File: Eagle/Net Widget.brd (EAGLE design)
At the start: 76.2 x 45.7 mm, 19 parts, among them IC1 ATmega1284P

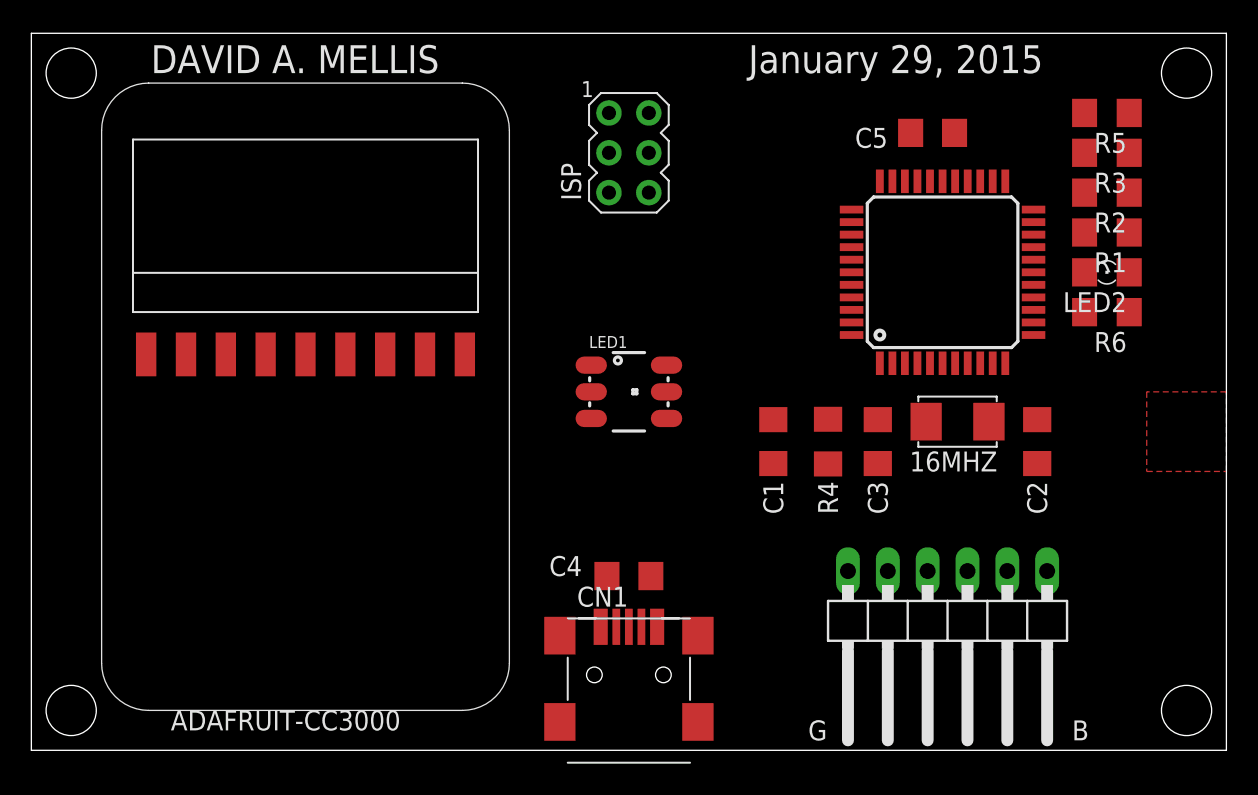
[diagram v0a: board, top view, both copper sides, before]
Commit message: Re-arrange LEDs and touch point.
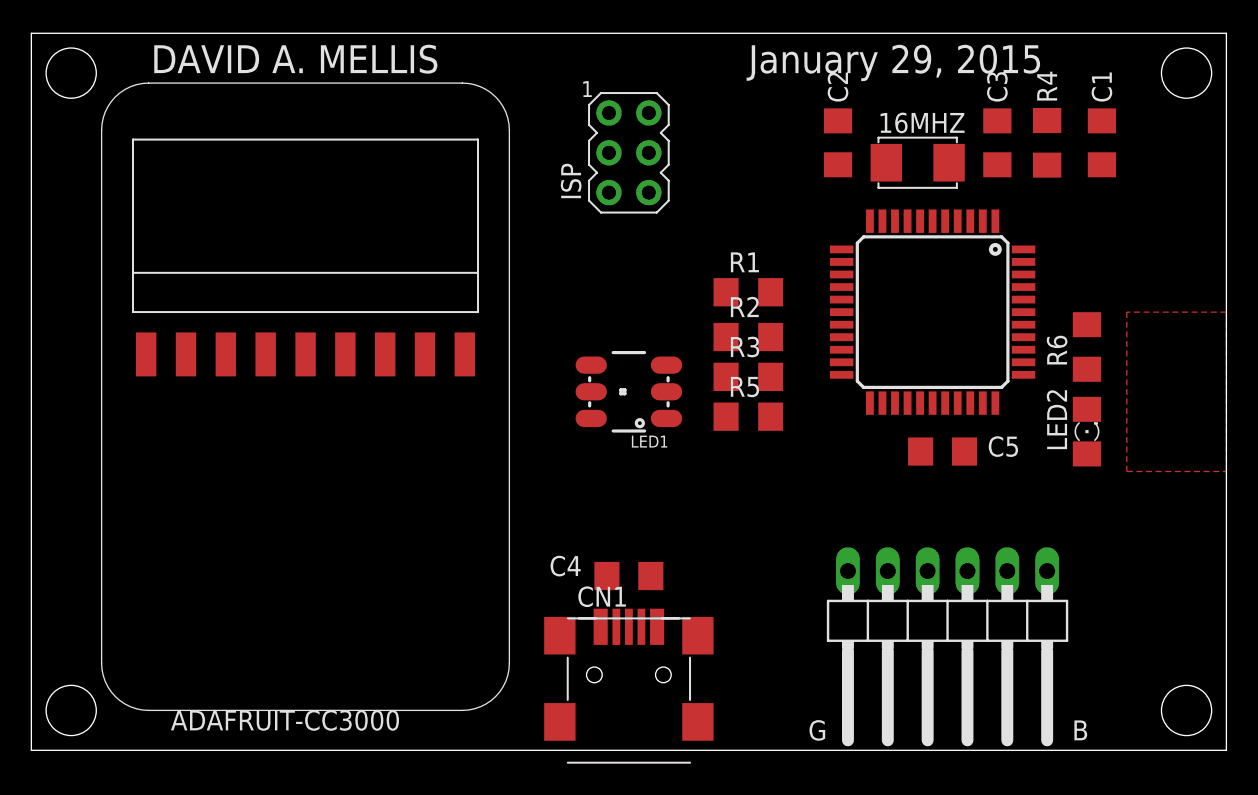
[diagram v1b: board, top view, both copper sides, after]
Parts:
- moved R5 30.0 mm to (45.7, 21.3), turned to 0 degrees
- moved C1 28.3 mm to (68.3, 38.7), turned to 90 degrees
- moved R3 27.0 mm to (45.7, 23.8), turned to 0 degrees
- moved R2 24.6 mm to (45.7, 26.4), turned to 0 degrees
- moved R4 23.6 mm to (64.8, 38.7), turned to 90 degrees
- moved R1 23.2 mm to (45.7, 29.2), turned to 0 degrees
- moved C2 22.9 mm to (51.4, 38.7), turned to 270 degrees
- moved C3 20.5 mm to (61.6, 38.7), turned to 270 degrees
- moved C5 20.3 mm to (58.1, 19.1), turned to 0 degrees
- moved 16MHZ 16.7 mm to (56.5, 37.5), turned to 0 degrees
- moved LED2 10.2 mm to (67.3, 20.3), turned to 90 degrees
- moved IC1 2.62 mm to (57.5, 27.9), turned to 270 degrees
- moved R6 2.56 mm to (67.3, 25.7), turned to 90 degrees
- turned LED1 to 180 degrees
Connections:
- removed net N$10: LED1.2, R2.1
- removed net N$11: LED1.1, R3.1
- removed net N$12: LED1.3, R5.1
- new net N$2: LED1.2, R3.1
- new net N$4: LED1.1, R5.1
- new net N$5: LED1.3, R2.1
- net B: now also IC1.14, R2.2; no longer IC1.16, R5.2
- net G: now also IC1.16, R5.2; no longer IC1.15, R3.2
- net N$1: now also IC1.35; no longer IC1.11
- net R: now also IC1.15, R3.2; no longer IC1.14, R2.2
- net TOUCH: now also IC1.34; no longer IC1.12

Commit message: Ditto.
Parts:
- moved LED2 12.0 mm to (71.8, 31.4), turned to 0 degrees
- moved R6 1.85 mm to (68.3, 24.1), turned to 180 degrees
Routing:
- net GND: track 0.00 -> 10.2 mm
- net TOUCH: track 0.00 -> 10.0 mm
- net N$1: track 0.00 -> 4.18 mm
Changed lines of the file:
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@@
 <element name="CN1" library="Net Widget" package="USB-MINIB-POWER" value="" x="38.1" y="2.54"/>
 <element name="LED1" library="SparkFun-LED" package="LED-TRICOLOR-5050" value="LED-TRICOLOR-5050NO_IC" x="38.1" y="22.86" rot="R180"/>
-<element name="LED2" library="led" package="1206" value="" x="67.31" y="20.32" rot="R90"/>
+<element name="LED2" library="led" package="1206" value="" x="71.755" y="31.4325"/>
 <element name="R1" library="rcl" package="R1206" value="100" x="45.72" y="29.21"/>
 <element name="R2" library="rcl" package="R1206" value="100" x="45.72" y="26.3525"/>
 <element name="R3" library="rcl" package="R1206" value="100" x="45.72" y="23.8125"/>
 <element name="R5" library="rcl" package="R1206" value="100" x="45.72" y="21.2725"/>
-<element name="R6" library="rcl" package="R1206" value="1M" x="67.31" y="25.7175" rot="R90"/>
+<element name="R6" library="rcl" package="R1206" value="1M" x="68.2625" y="24.13" rot="R180"/>
 </elements>
 <signals>
@@
 <contactref element="LED1" pad="5"/>
 <contactref element="LED2" pad="C"/>
-<wire x1="51.6675" y1="27.14" x2="67.31" y2="21.742" width="0" layer="19" extent="1-1"/>
-<wire x1="57.4675" y1="22.14" x2="51.6675" y2="27.14" width="0" layer="19" extent="1-1"/>
-<wire x1="59.5025" y1="19.05" x2="57.4675" y2="22.14" width="0" layer="19" extent="1-1"/>
-<wire x1="63.2675" y1="27.94" x2="57.4675" y2="22.14" width="0" layer="19" extent="1-1"/>
+<wire x1="51.435" y1="40.135" x2="61.595" y2="40.135" width="0.4064" layer="1"/>
+<wire x1="63.2675" y1="27.94" x2="73.177" y2="31.4325" width="0" layer="19" extent="1-1"/>
 <wire x1="57.4675" y1="33.74" x2="63.2675" y2="27.94" width="0" layer="19" extent="1-1"/>
 <wire x1="61.595" y1="40.135" x2="57.4675" y2="33.74" width="0" layer="19" extent="1-1"/>
-<wire x1="51.435" y1="40.135" x2="57.4675" y2="33.74" width="0" layer="19" extent="1-1"/>
-<wire x1="64.77" y1="11.43" x2="51.435" y2="40.135" width="0" layer="19" extent="1-1"/>
-<wire x1="35.7" y1="21.16" x2="63.2675" y2="27.94" width="0" layer="19" extent="1-1"/>
-<wire x1="35.7" y1="22.86" x2="35.7" y2="21.16" width="0" layer="19" extent="1-1"/>
-<wire x1="35.7" y1="24.56" x2="35.7" y2="22.86" width="0" layer="19" extent="1-1"/>
-<wire x1="39.5" y1="11.1125" x2="35.7" y2="24.56" width="0" layer="19" extent="1-1"/>
+<wire x1="57.4675" y1="22.14" x2="63.2675" y2="27.94" width="0" layer="19" extent="1-1"/>
+<wire x1="59.5025" y1="19.05" x2="57.4675" y2="22.14" width="0" layer="19" extent="1-1"/>
+<wire x1="51.6675" y1="27.14" x2="57.4675" y2="22.14" width="0" layer="19" extent="1-1"/>
+<wire x1="64.77" y1="11.43" x2="59.5025" y2="19.05" width="0" layer="19" extent="1-1"/>
+<wire x1="39.37" y1="35.56" x2="51.435" y2="40.135" width="0" layer="19" extent="1-1"/>
+<wire x1="35.7" y1="24.56" x2="39.37" y2="35.56" width="0" layer="19" extent="1-1"/>
+<wire x1="35.7" y1="22.86" x2="35.7" y2="24.56" width="0" layer="19" extent="1-1"/>
+<wire x1="35.7" y1="21.16" x2="35.7" y2="22.86" width="0" layer="19" extent="1-1"/>
+<wire x1="27.64" y1="25.245" x2="35.7" y2="24.56" width="0" layer="19" extent="1-1"/>
+<wire x1="39.5" y1="11.1125" x2="35.7" y2="21.16" width="0" layer="19" extent="1-1"/>
 <wire x1="39.9" y1="7.874" x2="39.5" y2="11.1125" width="0" layer="19" extent="1-1"/>
-<wire x1="39.37" y1="35.56" x2="35.7" y2="21.16" width="0" layer="19" extent="1-1"/>
-<wire x1="27.64" y1="25.245" x2="35.7" y2="21.16" width="0" layer="19" extent="1-1"/>
 </signal>
 <signal name="VCC" class="1">
@@
 <contactref element="JP5" pad="3"/>
 <contactref element="CN1" pad="VBUS"/>
+<wire x1="58.2675" y1="33.74" x2="64.77" y2="40.157" width="0" layer="19" extent="1-1"/>
+<wire x1="63.2675" y1="27.14" x2="58.2675" y2="33.74" width="0" layer="19" extent="1-1"/>
+<wire x1="56.6675" y1="22.14" x2="63.2675" y2="27.14" width="0" layer="19" extent="1-1"/>
 <wire x1="56.7025" y1="19.05" x2="56.6675" y2="22.14" width="0" layer="19" extent="1-1"/>
 <wire x1="51.6675" y1="27.94" x2="56.6675" y2="22.14" width="0" layer="19" extent="1-1"/>
-<wire x1="63.2675" y1="27.14" x2="56.6675" y2="22.14" width="0" layer="19" extent="1-1"/>
-<wire x1="58.2675" y1="33.74" x2="63.2675" y2="27.14" width="0" layer="19" extent="1-1"/>
-<wire x1="64.77" y1="40.157" x2="58.2675" y2="33.74" width="0" layer="19" extent="1-1"/>
-<wire x1="59.69" y1="11.43" x2="64.77" y2="40.157" width="0" layer="19" extent="1-1"/>
-<wire x1="36.7" y1="11.1125" x2="64.77" y2="40.157" width="0" layer="19" extent="1-1"/>
+<wire x1="59.69" y1="11.43" x2="56.7025" y2="19.05" width="0" layer="19" extent="1-1"/>
+<wire x1="39.37" y1="40.64" x2="51.6675" y2="27.94" width="0" layer="19" extent="1-1"/>
+<wire x1="36.7" y1="11.1125" x2="56.7025" y2="19.05" width="0" layer="19" extent="1-1"/>
 <wire x1="36.3" y1="7.874" x2="36.7" y2="11.1125" width="0" layer="19" extent="1-1"/>
-<wire x1="39.37" y1="40.64" x2="63.2675" y2="27.14" width="0" layer="19" extent="1-1"/>
 <wire x1="22.56" y1="25.245" x2="36.7" y2="11.1125" width="0" layer="19" extent="1-1"/>
 </signal>
@@
 <contactref element="R4" pad="1"/>
 <contactref element="C1" pad="1"/>
-<wire x1="64.77" y1="37.313" x2="59.0675" y2="33.74" width="0" layer="19" extent="1-1"/>
-<wire x1="68.2625" y1="37.335" x2="64.77" y2="37.313" width="0" layer="19" extent="1-1"/>
-<wire x1="36.83" y1="35.56" x2="68.2625" y2="37.335" width="0" layer="19" extent="1-1"/>
+<wire x1="64.77" y1="37.313" x2="68.2625" y2="37.335" width="0" layer="19" extent="1-1"/>
+<wire x1="59.0675" y1="33.74" x2="64.77" y2="37.313" width="0" layer="19" extent="1-1"/>
+<wire x1="36.83" y1="35.56" x2="59.0675" y2="33.74" width="0" layer="19" extent="1-1"/>
 </signal>
 <signal name="MOSI">
@@
 <contactref element="ISP" pad="4"/>
 <contactref element="IC1" pad="1"/>
-<wire x1="61.4675" y1="33.74" x2="39.37" y2="38.1" width="0" layer="19" extent="1-1"/>
+<wire x1="39.37" y1="38.1" x2="61.4675" y2="33.74" width="0" layer="19" extent="1-1"/>
 <wire x1="14.94" y1="25.245" x2="39.37" y2="38.1" width="0" layer="19" extent="1-1"/>
 </signal>
@@
 <contactref element="ISP" pad="1"/>
 <contactref element="IC1" pad="2"/>
-<wire x1="60.6675" y1="33.74" x2="36.83" y2="40.64" width="0" layer="19" extent="1-1"/>
+<wire x1="36.83" y1="40.64" x2="60.6675" y2="33.74" width="0" layer="19" extent="1-1"/>
 <wire x1="17.48" y1="25.245" x2="36.83" y2="40.64" width="0" layer="19" extent="1-1"/>
 </signal>
@@
 <contactref element="IC1" pad="7"/>
 <contactref element="IC1" pad="7"/>
-<wire x1="58.515" y1="37.465" x2="56.6675" y2="33.74" width="0" layer="19" extent="1-1"/>
-<wire x1="61.595" y1="37.335" x2="58.515" y2="37.465" width="0" layer="19" extent="1-1"/>
+<wire x1="58.515" y1="37.465" x2="61.595" y2="37.335" width="0" layer="19" extent="1-1"/>
+<wire x1="56.6675" y1="33.74" x2="58.515" y2="37.465" width="0" layer="19" extent="1-1"/>
 </signal>
 <signal name="N$7">
@@
 <contactref element="IC1" pad="8"/>
 <contactref element="IC1" pad="8"/>
-<wire x1="54.515" y1="37.465" x2="51.435" y2="37.335" width="0" layer="19" extent="1-1"/>
+<wire x1="51.435" y1="37.335" x2="54.515" y2="37.465" width="0" layer="19" extent="1-1"/>
 <wire x1="55.8675" y1="33.74" x2="54.515" y2="37.465" width="0" layer="19" extent="1-1"/>
 </signal>
@@
 <contactref element="IC1" pad="13"/>
 <contactref element="R1" pad="2"/>
-<wire x1="51.6675" y1="31.14" x2="47.142" y2="29.21" width="0" layer="19" extent="1-1"/>
+<wire x1="47.142" y1="29.21" x2="51.6675" y2="31.14" width="0" layer="19" extent="1-1"/>
 </signal>
 <signal name="B">
 <contactref element="IC1" pad="14"/>
 <contactref element="R2" pad="2"/>
-<wire x1="51.6675" y1="30.34" x2="47.142" y2="26.3525" width="0" layer="19" extent="1-1"/>
+<wire x1="47.142" y1="26.3525" x2="51.6675" y2="30.34" width="0" layer="19" extent="1-1"/>
 </signal>
 <signal name="R">
 <contactref element="IC1" pad="15"/>
 <contactref element="R3" pad="2"/>
-<wire x1="51.6675" y1="29.54" x2="47.142" y2="23.8125" width="0" layer="19" extent="1-1"/>
+<wire x1="47.142" y1="23.8125" x2="51.6675" y2="29.54" width="0" layer="19" extent="1-1"/>
 </signal>
 <signal name="G">
 <contactref element="IC1" pad="16"/>
 <contactref element="R5" pad="2"/>
-<wire x1="51.6675" y1="28.74" x2="47.142" y2="21.2725" width="0" layer="19" extent="1-1"/>
+<wire x1="47.142" y1="21.2725" x2="51.6675" y2="28.74" width="0" layer="19" extent="1-1"/>
 </signal>
 <signal name="N$9">
 <contactref element="R1" pad="1"/>
 <contactref element="LED2" pad="A"/>
-<wire x1="44.298" y1="29.21" x2="67.31" y2="18.898" width="0" layer="19" extent="1-1"/>
+<wire x1="44.298" y1="29.21" x2="70.333" y2="31.4325" width="0" layer="19" extent="1-1"/>
 </signal>
 <signal name="TOUCH">
 <contactref element="R6" pad="1"/>
 <polygon width="0.4064" layer="1">
-<vertex x="76.2" y="27.94"/>
-<vertex x="69.85" y="27.94"/>
-<vertex x="69.85" y="17.78"/>
+<vertex x="76.2" y="29.21"/>
+<vertex x="68.8975" y="29.21"/>
+<vertex x="68.8975" y="17.78"/>
 <vertex x="76.2" y="17.78"/>
 </polygon>
 <contactref element="IC1" pad="34"/>
-<wire x1="67.31" y1="24.2955" x2="63.2675" y2="23.94" width="0" layer="19" extent="1-1"/>
+<wire x1="63.2675" y1="23.94" x2="64.77" y2="23.94" width="0.3048" layer="1"/>
+<wire x1="64.77" y1="23.94" x2="64.77" y2="22.225" width="0.3048" layer="1"/>
+<wire x1="64.77" y1="22.225" x2="69.6845" y2="22.225" width="0.3048" layer="1"/>
+<wire x1="69.6845" y1="22.225" x2="69.6845" y2="24.13" width="0.3048" layer="1"/>
 </signal>
 <signal name="N$1">
 <contactref element="IC1" pad="35"/>
 <contactref element="R6" pad="2"/>
-<wire x1="67.31" y1="27.1395" x2="63.2675" y2="24.74" width="0" layer="19" extent="1-1"/>
+<wire x1="63.2675" y1="24.74" x2="66.8405" y2="24.74" width="0.3048" layer="1"/>
+<wire x1="66.8405" y1="24.74" x2="66.8405" y2="24.13" width="0.3048" layer="1"/>
 </signal>
 <signal name="N$2">

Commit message: More tweaks.
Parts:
- moved C1 27.2 mm to (52.1, 16.8), turned to 270 degrees
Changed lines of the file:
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@@
 <layer number="43" name="vRestrict" color="2" fill="10" visible="no" active="yes"/>
 <layer number="44" name="Drills" color="7" fill="1" visible="no" active="yes"/>
-<layer number="45" name="Holes" color="7" fill="1" visible="yes" active="yes"/>
+<layer number="45" name="Holes" color="7" fill="1" visible="no" active="yes"/>
 <layer number="46" name="Milling" color="3" fill="1" visible="no" active="yes"/>
 <layer number="47" name="Measures" color="7" fill="1" visible="no" active="yes"/>
@@
 <layer number="49" name="Reference" color="7" fill="1" visible="no" active="yes"/>
 <layer number="50" name="dxf" color="7" fill="1" visible="no" active="no"/>
-<layer number="51" name="tDocu" color="7" fill="1" visible="yes" active="yes"/>
+<layer number="51" name="tDocu" color="7" fill="1" visible="no" active="yes"/>
 <layer number="52" name="bDocu" color="7" fill="1" visible="no" active="yes"/>
 <layer number="53" name="tGND_GNDA" color="7" fill="9" visible="no" active="no"/>
@@
 <vertex x="56.8325" y="35.56"/>
 <vertex x="62.23" y="35.56"/>
+</polygon>
+<rectangle x1="69.85" y1="17.78" x2="76.2" y2="29.21" layer="41"/>
+<polygon width="0.4064" layer="42">
+<vertex x="76.2" y="29.21"/>
+<vertex x="69.85" y="29.21"/>
+<vertex x="69.85" y="25.0825"/>
+<vertex x="62.23" y="25.0825"/>
+<vertex x="62.23" y="23.495"/>
+<vertex x="64.4525" y="23.495"/>
+<vertex x="64.4525" y="21.9075"/>
+<vertex x="69.85" y="21.9075"/>
+<vertex x="69.85" y="17.78"/>
+<vertex x="76.2" y="17.78"/>
 </polygon>
 </plain>
@@
 <attribute name="VALUE" x="66.675" y="8.89" size="1.27" layer="27" rot="SR270"/>
 </element>
-<element name="C1" library="rcl" package="C1206" value="0.1uF" x="68.2625" y="38.735" smashed="yes" rot="R90">
-<attribute name="NAME" x="68.8975" y="41.275" size="1.27" layer="25" rot="R90"/>
-<attribute name="VALUE" x="70.8025" y="36.195" size="1.27" layer="27" rot="R90"/>
+<element name="C1" library="rcl" package="C1206" value="0.1uF" x="52.07" y="16.8275" smashed="yes" rot="R270">
+<attribute name="NAME" x="51.435" y="14.2875" size="1.27" layer="25" rot="R270"/>
+<attribute name="VALUE" x="49.53" y="19.3675" size="1.27" layer="27" rot="R270"/>
 </element>
 <element name="CN1" library="Net Widget" package="USB-MINIB-POWER" value="" x="38.1" y="2.54"/>
@@
 <contactref element="R4" pad="1"/>
 <contactref element="C1" pad="1"/>
-<wire x1="64.77" y1="37.313" x2="68.2625" y2="37.335" width="0" layer="19" extent="1-1"/>
+<wire x1="64.77" y1="37.313" x2="52.07" y2="18.2275" width="0" layer="19" extent="1-1"/>
 <wire x1="59.0675" y1="33.74" x2="64.77" y2="37.313" width="0" layer="19" extent="1-1"/>
 <wire x1="36.83" y1="35.56" x2="59.0675" y2="33.74" width="0" layer="19" extent="1-1"/>
@@
 <contactref element="JP5" pad="6"/>
 <contactref element="C1" pad="2"/>
-<wire x1="52.07" y1="11.43" x2="68.2625" y2="40.135" width="0" layer="19" extent="1-1"/>
+<wire x1="52.07" y1="11.43" x2="52.07" y2="15.4275" width="0" layer="19" extent="1-1"/>
 </signal>
 <signal name="RX">
@@
 <polygon width="0.4064" layer="1">
 <vertex x="76.2" y="29.21"/>
-<vertex x="68.8975" y="29.21"/>
-<vertex x="68.8975" y="17.78"/>
+<vertex x="69.85" y="29.21"/>
+<vertex x="69.85" y="17.78"/>
 <vertex x="76.2" y="17.78"/>
 </polygon>
